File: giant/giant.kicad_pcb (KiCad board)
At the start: 2 copper layers, 55 parts, among them IC1 MC7805BDTRKG, J1 Conn_01x02, J2 Conn_01x01, J3 Conn_01x06

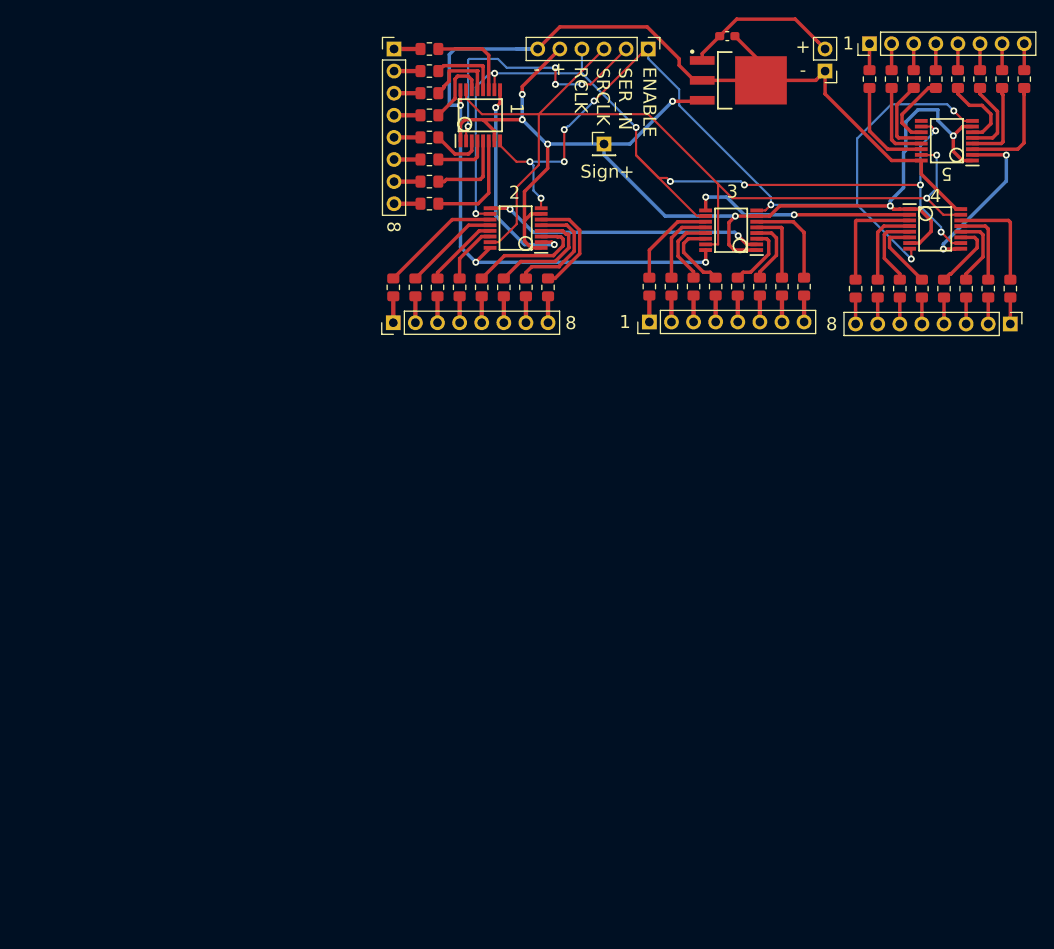
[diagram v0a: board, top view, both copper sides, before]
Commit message: Improved schematic layout for both cleanliness and programming ease
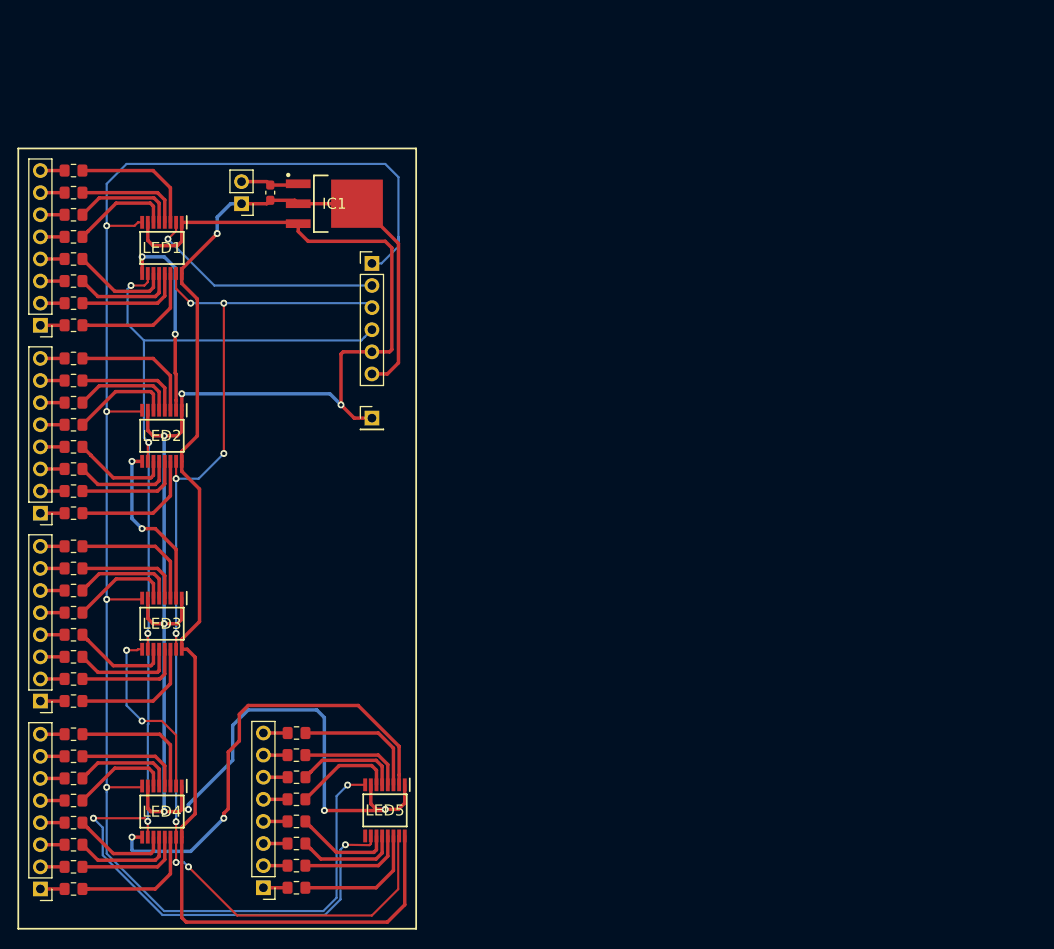
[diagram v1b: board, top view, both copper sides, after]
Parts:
- R1, R10, R11, R12, R13, R14, R15, R16, R17, R18, R19, R2, R20, R21, R22, R23, R24, R25, R26, R27, R28, R29, R3, R30, R31, R32, R33, R34, R35, R36, R37, R38, R39, R4, R40, R5, R6, R7, R8, R9: footprint Resistor_SMD:R_0805_2012Metric_Pad1.15x1.40mm_HandSolder -> NoText:R_0805_2012Metric_Pad1.15x1.40mm_HandSolder_noTEXT
- moved segment3 119.6 mm to (66.0, 139.7), turned to 180 degrees
- moved R24 117.6 mm to (69.8, 139.7), turned to 0 degrees
- moved R23 114.3 mm to (69.8, 137.2), turned to 0 degrees
- moved R9 113.9 mm to (69.8, 100.3), turned to 0 degrees
- moved R10 112.2 mm to (69.8, 102.9), turned to 0 degrees
- moved R22 111.0 mm to (69.8, 134.6), turned to 0 degrees
- moved R11 110.6 mm to (69.8, 105.4), turned to 0 degrees
- moved segment2 109.5 mm to (66.0, 118.1), turned to 180 degrees
- moved R12 109.1 mm to (69.8, 108.0), turned to 0 degrees
- moved R13 107.7 mm to (69.8, 110.5), turned to 0 degrees
- moved R21 107.6 mm to (69.8, 132.1), turned to 0 degrees
- moved R14 106.4 mm to (69.8, 113.0), turned to 0 degrees
- moved R15 105.3 mm to (69.8, 115.6), turned to 0 degrees
- moved R32 104.8 mm to (69.8, 161.3)
- moved segment4 104.7 mm to (66.0, 161.3), turned to 180 degrees
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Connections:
- LED1 pad 2: Net-(LED1-Pad2) -> Net-(J3-Pad2)
- LED2 pad 2: Net-(LED2-Pad2) -> Net-(LED1-Pad9)
- LED3 pad 2: Net-(LED1-Pad9) -> Net-(LED2-Pad9)
- LED3 pad 9: Net-(LED2-Pad2) -> Net-(LED3-Pad9)
- LED4 pad 2: Net-(J3-Pad2) -> Net-(LED3-Pad9)
- LED5 pad 9: Net-(LED1-Pad2) -> Net-(LED5-Pad9)
- R1 pad 2: Net-(LED1-Pad6) -> Net-(LED1-Pad3)
- R2 pad 2: Net-(LED1-Pad5) -> Net-(LED1-Pad4)
- R25 pad 2: Net-(LED4-Pad6) -> Net-(LED4-Pad3)
- R26 pad 2: Net-(LED4-Pad5) -> Net-(LED4-Pad4)
- R27 pad 2: Net-(LED4-Pad4) -> Net-(LED4-Pad5)
- R28 pad 2: Net-(LED4-Pad3) -> Net-(LED4-Pad6)
- R29 pad 2: Net-(LED4-Pad14) -> Net-(LED4-Pad11)
- R3 pad 2: Net-(LED1-Pad4) -> Net-(LED1-Pad5)
- R30 pad 2: Net-(LED4-Pad13) -> Net-(LED4-Pad12)
- R31 pad 2: Net-(LED4-Pad12) -> Net-(LED4-Pad13)
- R32 pad 2: Net-(LED4-Pad11) -> Net-(LED4-Pad14)
- R33 pad 2: Net-(LED5-Pad6) -> Net-(LED5-Pad3)
- R34 pad 2: Net-(LED5-Pad5) -> Net-(LED5-Pad4)
- R35 pad 2: Net-(LED5-Pad4) -> Net-(LED5-Pad5)
- R36 pad 2: Net-(LED5-Pad3) -> Net-(LED5-Pad6)
- R37 pad 2: Net-(LED5-Pad14) -> Net-(LED5-Pad11)
- R38 pad 2: Net-(LED5-Pad13) -> Net-(LED5-Pad12)
- R39 pad 2: Net-(LED5-Pad12) -> Net-(LED5-Pad13)
- R4 pad 2: Net-(LED1-Pad3) -> Net-(LED1-Pad6)
- R40 pad 2: Net-(LED5-Pad11) -> Net-(LED5-Pad14)
- R5 pad 2: Net-(LED1-Pad14) -> Net-(LED1-Pad11)
- R6 pad 2: Net-(LED1-Pad13) -> Net-(LED1-Pad12)
- R7 pad 2: Net-(LED1-Pad12) -> Net-(LED1-Pad13)
- R8 pad 2: Net-(LED1-Pad11) -> Net-(LED1-Pad14)
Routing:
- net Net-(J3-Pad1): track 100.6 -> 186.5 mm, vias 8 -> 5
- net Net-(IC1-Pad3): track 142.5 -> 204.5 mm, vias 7 -> 8
- net Net-(J3-Pad4): track 108.7 -> 151.0 mm, vias 8 -> 6
- net Net-(LED1-Pad2): track 32.4 -> 0.00 mm, vias 2 -> 0
- net Net-(LED4-Pad9): track 24.4 -> 52.7 mm
- net Net-(J3-Pad3): track 107.2 -> 132.7 mm, vias 2 -> 8
- net Net-(C1-Pad1): track 139.0 -> 162.5 mm, vias 3 -> 1
- net Net-(LED3-Pad9): track 0.00 -> 21.1 mm, vias 0 -> 2
- net Net-(LED2-Pad9): track 0.00 -> 19.9 mm, vias 0 -> 2
- net Net-(LED2-Pad2): track 19.7 -> 0.00 mm, vias 2 -> 0
- net Net-(C1-Pad2): track 18.0 -> 6.75 mm
- net Net-(LED4-Pad3): track 5.92 -> 15.3 mm
- net Net-(LED5-Pad14): track 6.83 -> 14.9 mm
- net Net-(LED4-Pad14): track 8.37 -> 15.7 mm
- net Net-(LED1-Pad3): track 7.68 -> 14.9 mm
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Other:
- board text removed: "+"
- board text removed: "-"
- board text removed: "1"
- board text removed: "2"
- board text removed: "3"
- board text removed: "4"
- board text removed: "5"
- board text removed: "8"
- board text removed: "ENABLE"
- board text removed: "RCLK"
- board text removed: "SER_IN"
- board text removed: "SRCLK"
- board text removed: "Sign+"

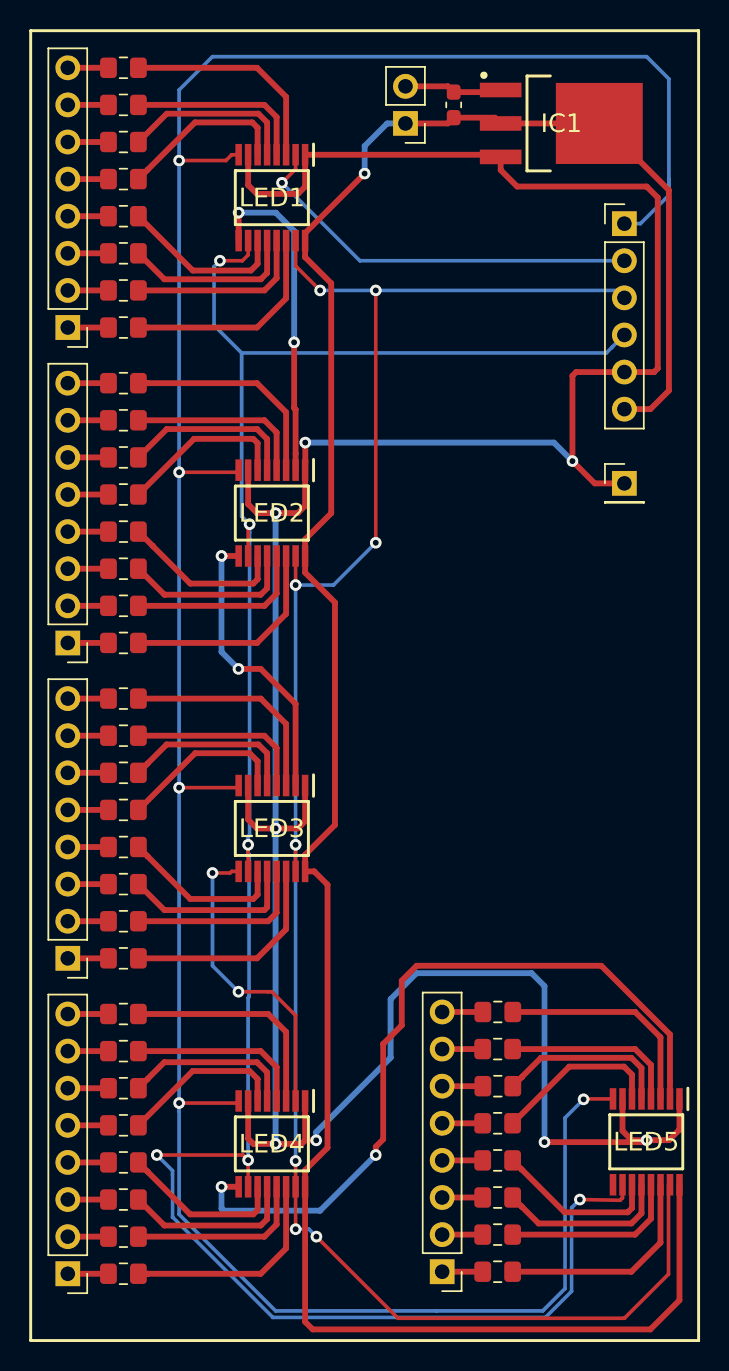
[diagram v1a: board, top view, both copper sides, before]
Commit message: Added text and updated 3d view
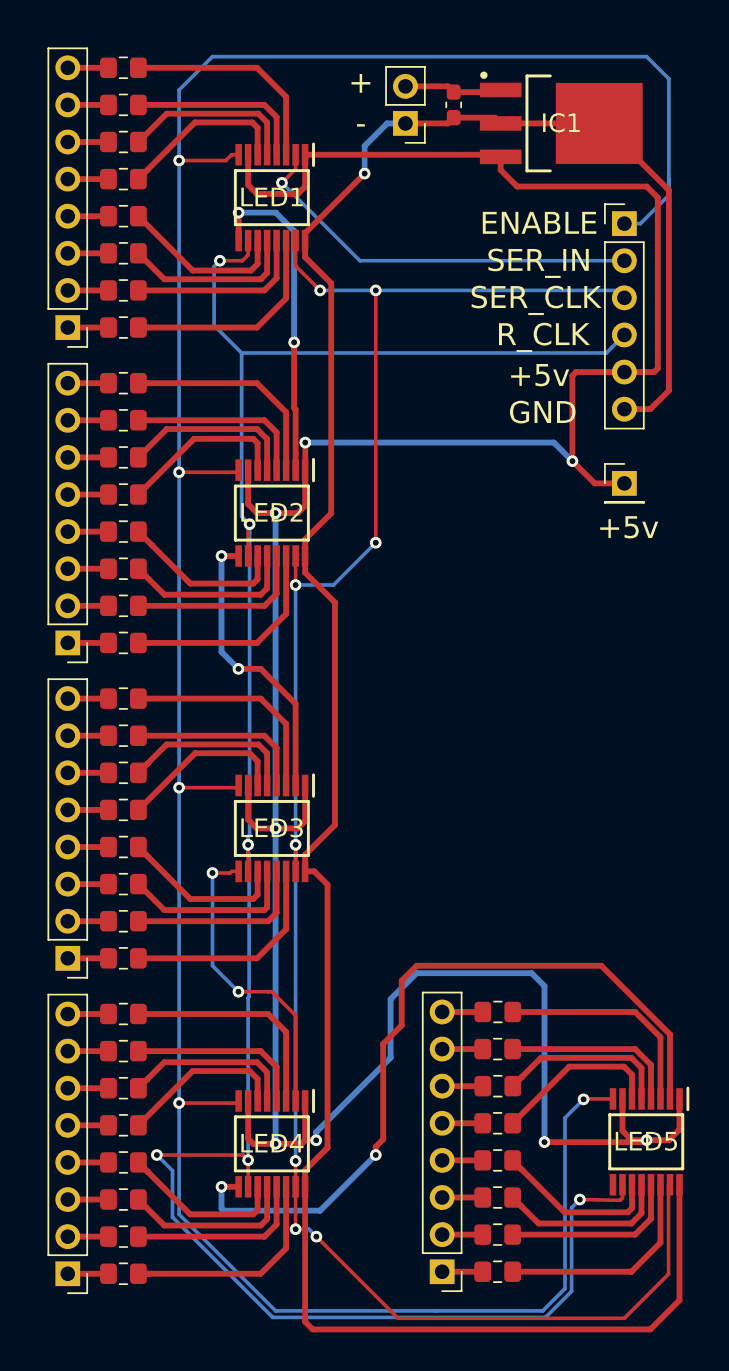
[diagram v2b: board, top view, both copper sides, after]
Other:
- board text added: "+"
- board text added: "+5v"
- board text added: "-"
- board text added: "ENABLE"
- board text added: "GND"
- board text added: "R_CLK"
- board text added: "SER_CLK"
- board text added: "SER_IN"
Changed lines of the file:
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@@
   (general
     (thickness 1.6)
-    (drawings 4)
+    (drawings 9)
     (tracks 507)
     (zones 0)
@@
     (pad 16 smd rect (at 2.938 -2.275) (size 0.45 1.475) (layers F.Cu F.Paste F.Mask)
       (net 85 "Net-(C1-Pad1)"))
+    (model ${KISYS3DMOD}/Package_SO.3dshapes/TSSOP-16-1EP_4.4x5mm_P0.65mm.step
+      (at (xyz 0 0 0))
+      (scale (xyz 1 1 1))
+      (rotate (xyz 0 0 0))
+    )
   )
   (module SOP65P640X120-16N (layer F.Cu)
@@
     (pad 1 smd rect (at -2.938 -2.275) (size 0.45 1.475) (layers F.Cu F.Paste F.Mask)
       (net 86 "Net-(IC1-Pad3)"))
+    (model ${KISYS3DMOD}/Package_SO.3dshapes/TSSOP-16-1EP_4.4x5mm_P0.65mm.step
+      (at (xyz 0 0 0))
+      (scale (xyz 1 1 1))
+      (rotate (xyz 0 0 0))
+    )
   )
   (module SOP65P640X120-16N (layer F.Cu)
@@
     (pad 16 smd rect (at 2.938 -2.275) (size 0.45 1.475) (layers F.Cu F.Paste F.Mask)
       (net 85 "Net-(C1-Pad1)"))
+    (model ${KISYS3DMOD}/Package_SO.3dshapes/TSSOP-16-1EP_4.4x5mm_P0.65mm.step
+      (at (xyz 0 0 0))
+      (scale (xyz 1 1 1))
+      (rotate (xyz 0 0 0))
+    )
   )
   (module SOP65P640X120-16N (layer F.Cu)
@@
     (pad 1 smd rect (at -2.938 -2.275) (size 0.45 1.475) (layers F.Cu F.Paste F.Mask)
       (net 86 "Net-(IC1-Pad3)"))
+    (model ${KISYS3DMOD}/Package_SO.3dshapes/TSSOP-16-1EP_4.4x5mm_P0.65mm.step
+      (at (xyz 0 0 0))
+      (scale (xyz 1 1 1))
+      (rotate (xyz 0 0 0))
+    )
   )
   (module SOP65P640X120-16N (layer F.Cu)
@@
     (pad 16 smd rect (at 2.938 -2.275) (size 0.45 1.475) (layers F.Cu F.Paste F.Mask)
       (net 85 "Net-(C1-Pad1)"))
+    (model ${KISYS3DMOD}/Package_SO.3dshapes/TSSOP-16-1EP_4.4x5mm_P0.65mm.step
+      (at (xyz 0 0 0))
+      (scale (xyz 1 1 1))
+      (rotate (xyz 0 0 0))
+    )
   )
   (module TO229P990X238-4N (layer F.Cu)
@@
     (pad 4 smd rect (at 2.6 0 90) (size 5.55 5.95) (layers F.Cu F.Paste F.Mask)
       (net 85 "Net-(C1-Pad1)"))
+    (model ${KISYS3DMOD}/Package_TO_SOT_SMD.3dshapes/TO-252-2.step
+      (at (xyz 0 0 0))
+      (scale (xyz 1 1 1))
+      (rotate (xyz 0 0 0))
+    )
   )
   (module Capacitor_SMD:C_0603_1608Metric_Pad1.05x0.95mm_HandSolder (layer F.Cu)
@@
     )
   )
-  (gr_line (start 109.22 165.862) (end 63.5 165.862) (layer F.SilkS) (width 0.2))
-  (gr_line (start 109.22 76.2) (end 109.22 165.862) (layer F.SilkS) (width 0.2))
-  (gr_line (start 63.5 76.2) (end 109.22 76.2) (layer F.SilkS) (width 0.2))
-  (gr_line (start 63.5 76.2) (end 63.5 165.862) (layer F.SilkS) (width 0.2))
+  (gr_text "-\n" (at 86.106 82.55) (layer F.SilkS)
+    (effects (font (size 1.5 1.5) (thickness 0.3)))
+  )
+  (gr_text + (at 86.106 79.756) (layer F.SilkS)
+    (effects (font (size 1.5 1.5) (thickness 0.3)))
+  )
+  (gr_text +5v (at 104.394 110.236) (layer F.SilkS)
+    (effects (font (size 1.5 1.5) (thickness 0.3)))
+  )
+  (gr_text "GND\n" (at 98.552 102.362) (layer F.SilkS)
+    (effects (font (size 1.5 1.5) (thickness 0.3)))
+  )
+  (gr_text "+5v\n" (at 98.298 99.822) (layer F.SilkS)
+    (effects (font (size 1.5 1.5) (thickness 0.3)))
+  )
+  (gr_text "R_CLK\n" (at 98.552 97.028) (layer F.SilkS)
+    (effects (font (size 1.5 1.5) (thickness 0.3)))
+  )
+  (gr_text "SER_CLK\n" (at 98.044 94.488) (layer F.SilkS)
+    (effects (font (size 1.5 1.5) (thickness 0.3)))
+  )
+  (gr_text "SER_IN\n" (at 98.298 91.948) (layer F.SilkS)
+    (effects (font (size 1.5 1.5) (thickness 0.3)))
+  )
+  (gr_text ENABLE (at 98.298 89.408) (layer F.SilkS)
+    (effects (font (size 1.5 1.5) (thickness 0.3)))
+  )
   (segment (start 66.04 81.28) (end 68.825 81.28) (width 0.4) (layer F.Cu) (net 1))
   (segment (start 70.875 81.28) (end 79.502 81.28) (width 0.4) (layer F.Cu) (net 2))

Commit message: added gerber files and basic README
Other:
- board outline added: 45.2 x 89.7 mm
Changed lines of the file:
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@@
   (general
     (thickness 1.6)
-    (drawings 9)
+    (drawings 13)
     (tracks 507)
     (zones 0)
@@
     (visible_elements FFFFFF7F)
     (pcbplotparams
-      (layerselection 0x010fc_ffffffff)
+      (layerselection 0x010a8_ffffffff)
       (usegerberextensions false)
       (usegerberattributes false)
@@
       (outputformat 1)
       (mirror false)
-      (drillshape 1)
+      (drillshape 0)
       (scaleselection 1)
-      (outputdirectory ""))
+      (outputdirectory "../gerber/"))
   )
   (net 0 "")
@@
     )
   )
+  (gr_line (start 108.966 76.454) (end 63.754 76.454) (layer Edge.Cuts) (width 0.15))
+  (gr_line (start 108.966 166.116) (end 108.966 76.454) (layer Edge.Cuts) (width 0.15))
+  (gr_line (start 63.754 166.116) (end 108.966 166.116) (layer Edge.Cuts) (width 0.15))
+  (gr_line (start 63.754 76.454) (end 63.754 166.116) (layer Edge.Cuts) (width 0.15))
   (gr_text "-\n" (at 86.106 82.55) (layer F.SilkS)
     (effects (font (size 1.5 1.5) (thickness 0.3)))
